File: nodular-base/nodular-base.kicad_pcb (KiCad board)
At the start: 2 copper layers, 83.1 x 92.5 mm, 18 parts, among them J1 Conn_02x10_Counter_Clockwise, J2 Conn_02x10_Counter_Clockwise, J3 Conn_02x10_Counter_Clockwise, J4 Conn_02x10_Counter_Clockwise, J5 Conn_02x10_Counter_Clockwise, J6 Conn_02x10_Counter_Clockwise

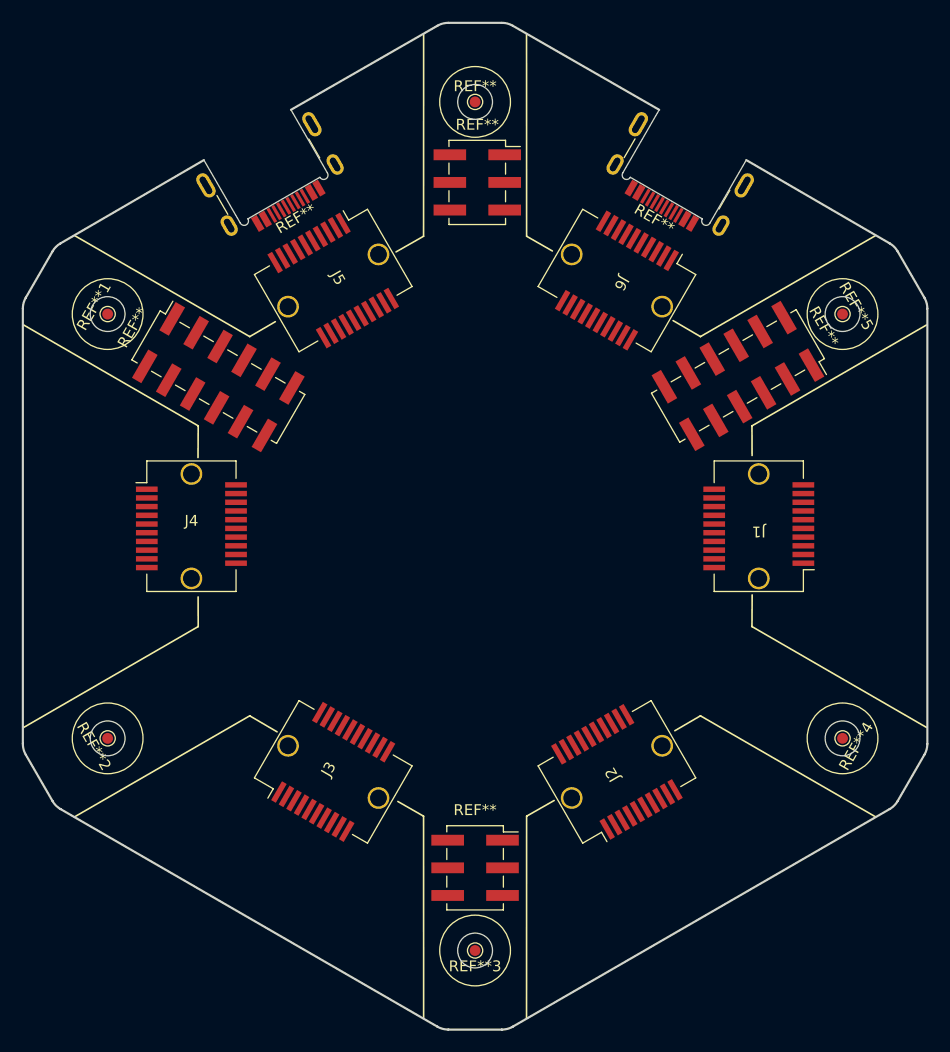
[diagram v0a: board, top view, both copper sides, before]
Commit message: more solderable standoffs, mid-mount USB
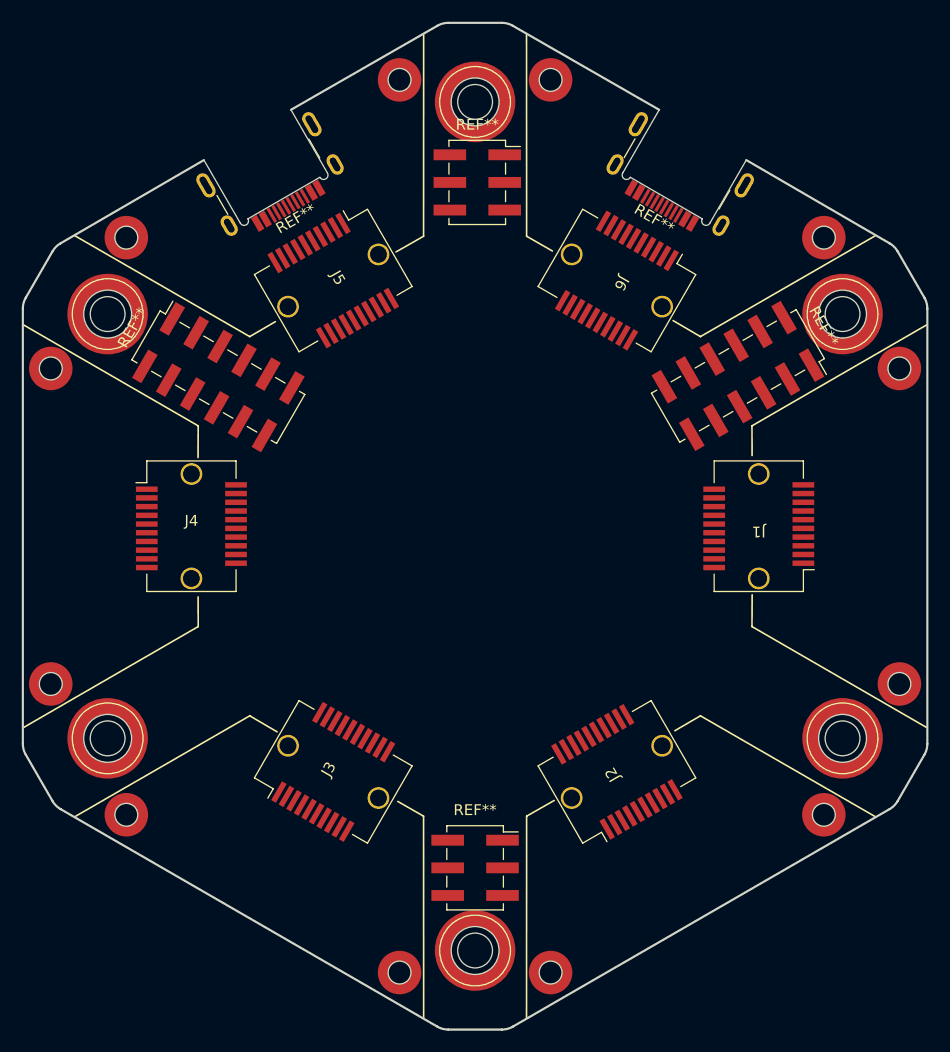
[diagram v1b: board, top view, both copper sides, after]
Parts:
- removed the REF** at (100.0, 61.0)
- added REF**: Mounting_Wuerth_WA-SMSI-M3_H12mm_9774120360, Mounting_Wuerth:Mounting_Wuerth_WA-SMSI-M3_H12mm_9774120360, F.Cu at (100.0, 61.0)
- added REF**: Mounting_Wuerth_WA-SMSI-M1.6_H2.5mm_9774025633, Mounting_Wuerth:Mounting_Wuerth_WA-SMSI-M1.6_H2.5mm_9774025633, F.Cu at (139.0, 114.5)
- added REF**: Mounting_Wuerth_WA-SMSI-M1.6_H2.5mm_9774025633, Mounting_Wuerth:Mounting_Wuerth_WA-SMSI-M1.6_H2.5mm_9774025633, F.Cu at (139.0, 85.5)
- added REF**10: Mounting_Wuerth_WA-SMSI-M1.6_H2.5mm_9774025633, Mounting_Wuerth:Mounting_Wuerth_WA-SMSI-M1.6_H2.5mm_9774025633, F.Cu at (61.0, 114.5)
- added REF**11: Mounting_Wuerth_WA-SMSI-M1.6_H2.5mm_9774025633, Mounting_Wuerth:Mounting_Wuerth_WA-SMSI-M1.6_H2.5mm_9774025633, F.Cu at (61.0, 85.5)
- added REF**12: Mounting_Wuerth_WA-SMSI-M1.6_H2.5mm_9774025633, Mounting_Wuerth:Mounting_Wuerth_WA-SMSI-M1.6_H2.5mm_9774025633, F.Cu at (93.1, 141.0)
- added REF**13: Mounting_Wuerth_WA-SMSI-M1.6_H2.5mm_9774025633, Mounting_Wuerth:Mounting_Wuerth_WA-SMSI-M1.6_H2.5mm_9774025633, F.Cu at (67.9, 126.5)
- added REF**14: Mounting_Wuerth_WA-SMSI-M1.6_H2.5mm_9774025633, Mounting_Wuerth:Mounting_Wuerth_WA-SMSI-M1.6_H2.5mm_9774025633, F.Cu at (106.9, 141.0)
- added REF**15: Mounting_Wuerth_WA-SMSI-M1.6_H2.5mm_9774025633, Mounting_Wuerth:Mounting_Wuerth_WA-SMSI-M1.6_H2.5mm_9774025633, F.Cu at (132.1, 126.5)
- added REF**6: Mounting_Wuerth_WA-SMSI-M1.6_H2.5mm_9774025633, Mounting_Wuerth:Mounting_Wuerth_WA-SMSI-M1.6_H2.5mm_9774025633, F.Cu at (132.1, 73.5)
- added REF**7: Mounting_Wuerth_WA-SMSI-M1.6_H2.5mm_9774025633, Mounting_Wuerth:Mounting_Wuerth_WA-SMSI-M1.6_H2.5mm_9774025633, F.Cu at (106.9, 59.0)
- added REF**8: Mounting_Wuerth_WA-SMSI-M1.6_H2.5mm_9774025633, Mounting_Wuerth:Mounting_Wuerth_WA-SMSI-M1.6_H2.5mm_9774025633, F.Cu at (67.9, 73.5)
- added REF**9: Mounting_Wuerth_WA-SMSI-M1.6_H2.5mm_9774025633, Mounting_Wuerth:Mounting_Wuerth_WA-SMSI-M1.6_H2.5mm_9774025633, F.Cu at (93.1, 59.0)
- REF**1, REF**2, REF**3, REF**4, REF**5: value TestPoint_Pad_D1.0mm -> Mounting_Wuerth_WA-SMSI-M3_H12mm_9774120360; footprint TestPoint:TestPoint_Pad_D1.0mm -> Mounting_Wuerth:Mounting_Wuerth_WA-SMSI-M3_H12mm_9774120360

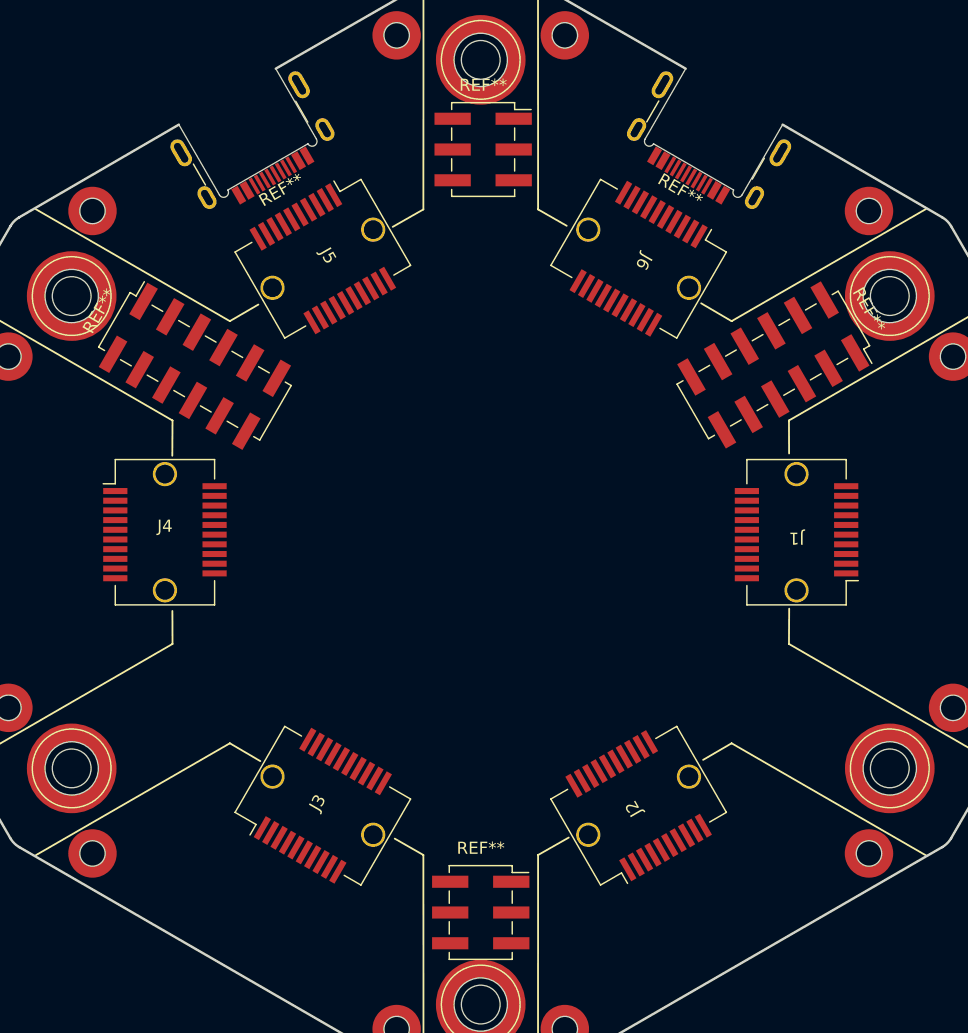
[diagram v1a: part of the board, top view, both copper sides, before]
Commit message: Update layout for top board, add library items
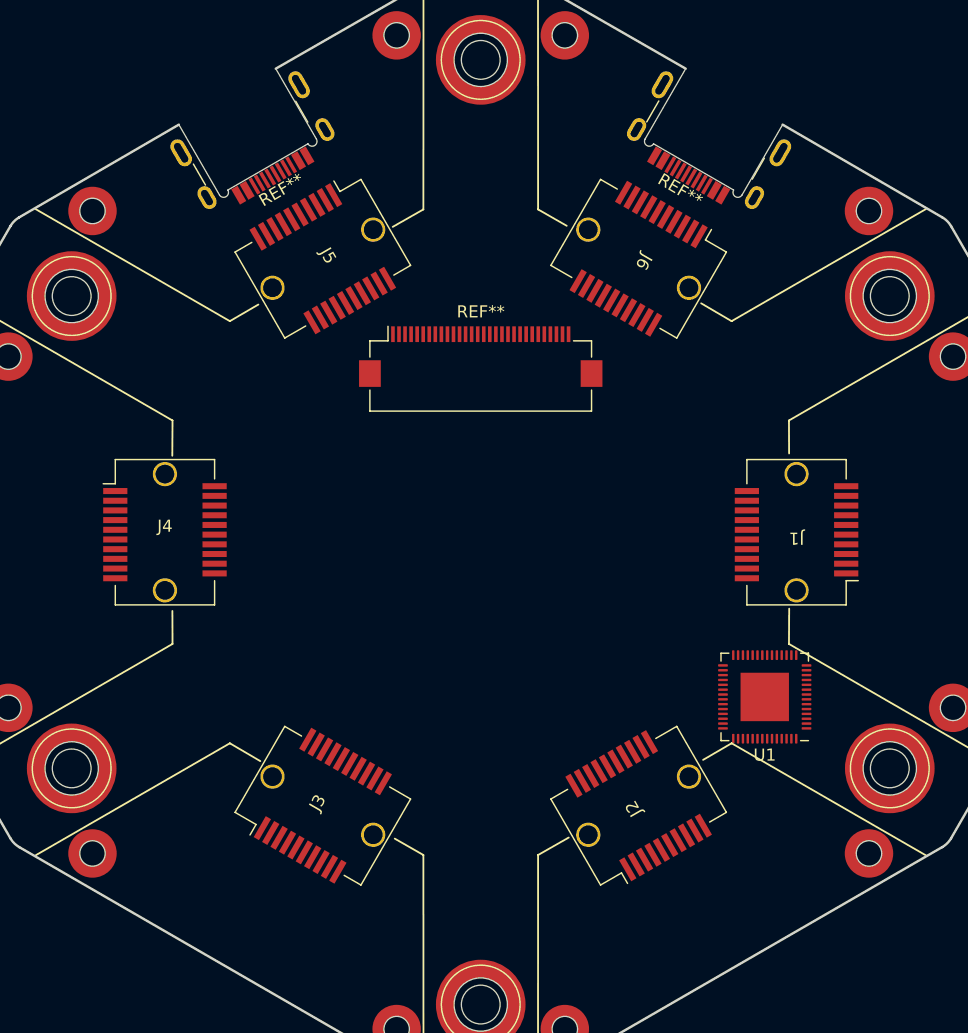
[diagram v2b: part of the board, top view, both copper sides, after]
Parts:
- removed the REF** at (124.2, 86.2)
- removed the REF** at (100.0, 131.4)
- removed the REF** at (100.2, 68.4)
- removed the REF** at (76.4, 86.3)
- added REF**: Hirose_FH12-30S-0.5SH_1x30-1MP_P0.50mm_Horizontal, Connector_FFC-FPC:Hirose_FH12-30S-0.5SH_1x30-1MP_P0.50mm_Horizontal, F.Cu at (100.0, 85.5)
- added U1: ESP32-S3-PICO-1-N8R2, Package_DFN_QFN:QFN-56-1EP_7x7mm_P0.4mm_EP4x4mm, F.Cu at (123.5, 113.6)
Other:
- board text added: "Display header top"

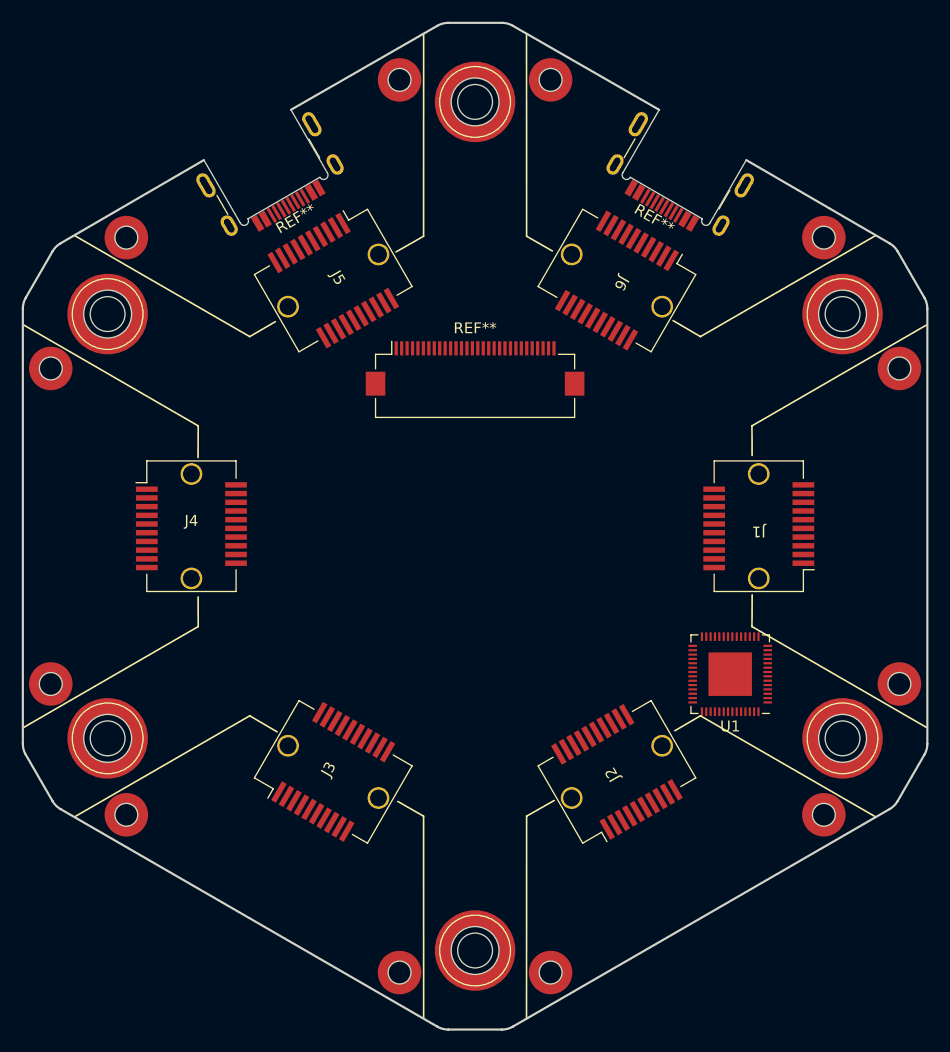
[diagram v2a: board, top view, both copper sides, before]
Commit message: Nodular-base: Add most components onto baseboard for a test fit. Nodular-base: Add fps and models for solderable standoffs, replace solderable standoffs and reposition them. Nodule template: Adjust nodule template hole position, export STEP of nodule. Nodular-base: Add many components to schematic, structure schematic hierarchy Nodular-base: Route USB, RF path, and MCU decoupling
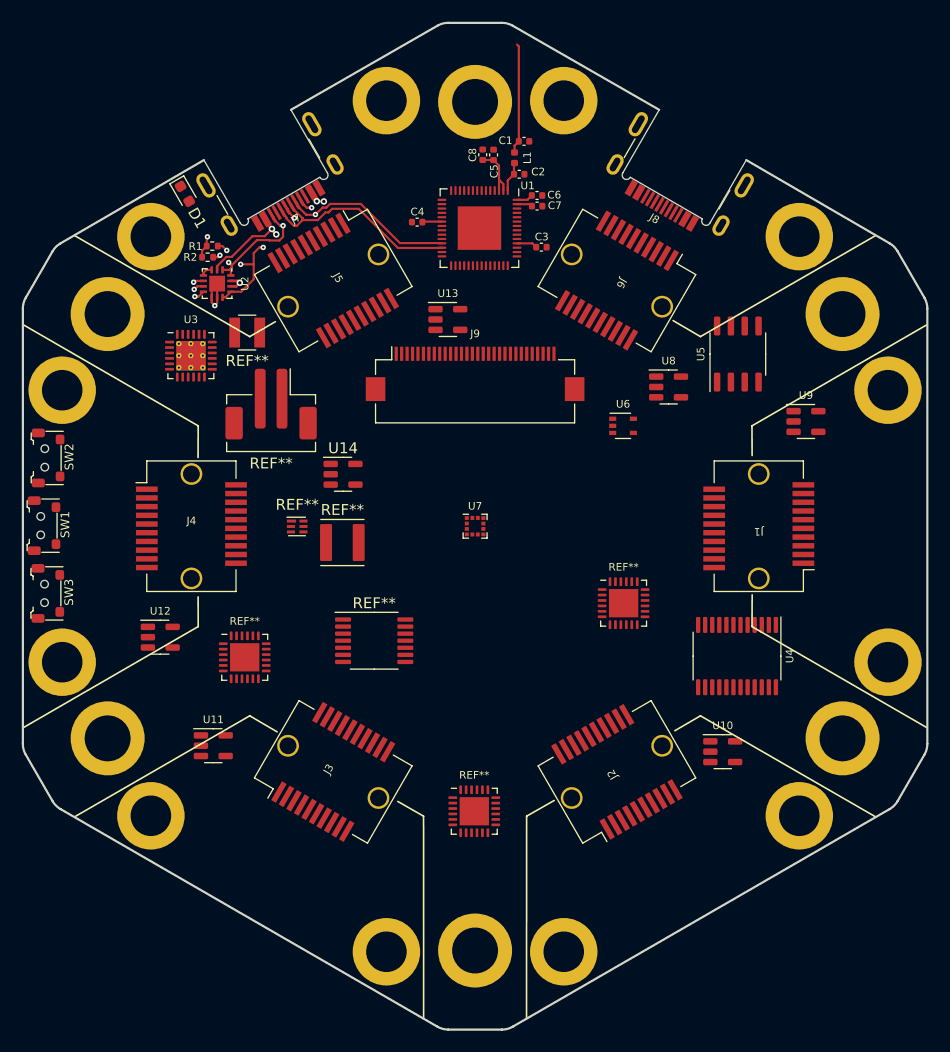
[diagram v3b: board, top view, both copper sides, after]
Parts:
- removed the REF** at (100.0, 85.5)
- removed the REF** at (100.0, 61.0)
- removed the REF** at (139.0, 114.5)
- removed the REF** at (139.0, 85.5)
- removed REF**1, REF**2, REF**3, REF**4, REF**5: Mounting_Wuerth_WA-SMSI-M3_H12mm_9774120360, Mounting_Wuerth:Mounting_Wuerth_WA-SMSI-M3_H12mm_9774120360
- removed REF**10, REF**11, REF**12, REF**13, REF**14, REF**15, REF**6, REF**7, REF**8, REF**9: Mounting_Wuerth_WA-SMSI-M1.6_H2.5mm_9774025633, Mounting_Wuerth:Mounting_Wuerth_WA-SMSI-M1.6_H2.5mm_9774025633
- added C1: C, Capacitor_SMD:C_0402_1005Metric, F.Cu at (104.5, 64.6)
- added C2: C, Capacitor_SMD:C_0402_1005Metric, F.Cu at (104.1, 67.7)
- added C3: 100nF, Capacitor_SMD:C_0402_1005Metric, F.Cu at (106.1, 74.3)
- added C4: 100nF, Capacitor_SMD:C_0402_1005Metric, F.Cu at (94.7, 72.0)
- added C5: 100nF, Capacitor_SMD:C_0402_1005Metric, F.Cu at (101.7, 65.9)
- added C6: 100nF, Capacitor_SMD:C_0402_1005Metric, F.Cu at (105.7, 69.6)
- added C7: 100nF, Capacitor_SMD:C_0402_1005Metric, F.Cu at (105.7, 70.6)
- added C8: 100nF, Capacitor_SMD:C_0402_1005Metric, F.Cu at (100.7, 65.9)
- added D1: LED, LED_SMD:LED_0603_1608Metric, F.Cu at (73.3, 69.5)
- added H1: MountingHole_Pad, nodular:SMTSO2030CTJ, F.Cu at (137.9, 87.5)
- added H10: MountingHole_Pad, nodular:SMTSO2030CTJ, F.Cu at (91.9, 60.9)
- added H11: MountingHole_Pad, nodular:SMTSO2030CTJ, F.Cu at (108.1, 60.9)
- added H12: MountingHole_Pad, nodular:SMTSO2030CTJ, F.Cu at (129.8, 73.4)
- added H13: MountingHole_Pad, nodular:SMTSO3030CTJ, F.Cu at (100.0, 61.0)
- added H14: MountingHole_Pad, nodular:SMTSO3030CTJ, F.Cu at (66.2, 80.5)
- added H15: MountingHole_Pad, nodular:SMTSO3030CTJ, F.Cu at (66.2, 119.5)
- added H16: MountingHole_Pad, nodular:SMTSO3030CTJ, F.Cu at (100.0, 139.0)
- added H17: MountingHole_Pad, nodular:SMTSO3030CTJ, F.Cu at (133.8, 119.5)
- added H18: MountingHole_Pad, nodular:SMTSO3030CTJ, F.Cu at (133.8, 80.5)
- added H2: MountingHole_Pad, nodular:SMTSO2030CTJ, F.Cu at (137.9, 112.5)
- added H3: MountingHole_Pad, nodular:SMTSO2030CTJ, F.Cu at (129.8, 126.6)
- added H4: MountingHole_Pad, nodular:SMTSO2030CTJ, F.Cu at (108.1, 139.1)
- added H5: MountingHole_Pad, nodular:SMTSO2030CTJ, F.Cu at (91.9, 139.1)
- added H6: MountingHole_Pad, nodular:SMTSO2030CTJ, F.Cu at (70.2, 126.6)
- added H7: MountingHole_Pad, nodular:SMTSO2030CTJ, F.Cu at (62.0, 112.5)
- added H8: MountingHole_Pad, nodular:SMTSO2030CTJ, F.Cu at (62.0, 87.5)
- added H9: MountingHole_Pad, nodular:SMTSO2030CTJ, F.Cu at (70.2, 73.4)
- added J9: Conn_01x30_MountingPin, Connector_FFC-FPC:Hirose_FH12-30S-0.5SH_1x30-1MP_P0.50mm_Horizontal, F.Cu at (100.0, 86.0)
- added L1: L, Inductor_SMD:L_0402_1005Metric, F.Cu at (103.6, 66.1)
- added R1: 5k1, Resistor_SMD:R_0402_1005Metric, F.Cu at (75.8, 74.2)
- added R2: 5k1, Resistor_SMD:R_0402_1005Metric, F.Cu at (75.4, 75.3)
- added REF**: QFN-24-1EP_4x4mm_P0.5mm_EP2.7x2.6mm, Package_DFN_QFN:QFN-24-1EP_4x4mm_P0.5mm_EP2.7x2.6mm, F.Cu at (99.9, 126.2)
- added REF**: WSON6_1.5x1.5mm_P0.5mm, Package_SON:WSON-6_1.5x1.5mm_P0.5mm, F.Cu at (83.7, 100.0)
- added REF**: TSSOP-14_4.4x5mm_P0.65mm, Package_SO:TSSOP-14_4.4x5mm_P0.65mm, F.Cu at (90.7, 110.5)
- added REF**: QFN-24-1EP_4x4mm_P0.5mm_EP2.7x2.6mm, Package_DFN_QFN:QFN-24-1EP_4x4mm_P0.5mm_EP2.7x2.6mm, F.Cu at (113.7, 107.1)
- added REF**: QFN-24-1EP_4x4mm_P0.5mm_EP2.7x2.6mm, Package_DFN_QFN:QFN-24-1EP_4x4mm_P0.5mm_EP2.7x2.6mm, F.Cu at (78.8, 112.0)
- added REF**: JST_PH_B2B-PH-SM4-TB_1x02-1MP_P2.00mm_Vertical, Connector_JST:JST_PH_B2B-PH-SM4-TB_1x02-1MP_P2.00mm_Vertical, F.Cu at (81.2, 88.8)
- added REF**: L_Abracon_ASPI-4030S, Inductor_SMD:L_Abracon_ASPI-4030S, F.Cu at (87.8, 101.5)
- added REF**: L_Abracon_ASPI-3012S, Inductor_SMD:L_Abracon_ASPI-3012S, F.Cu at (79.0, 82.2)
- added SW1: SW_Push, nodular:sidebutton-1TS003B-1400-3500A-CT, F.Cu at (60.1, 100.0)
- added SW2: SW_Push, nodular:sidebutton-1TS003B-1400-3500A-CT, F.Cu at (60.5, 93.7)
- added SW3: SW_Push, nodular:sidebutton-1TS003B-1400-3500A-CT, F.Cu at (60.4, 106.2)
- added U10: MT9700, Package_TO_SOT_SMD:SOT-23-5, F.Cu at (122.8, 120.7)
- added U11: MT9700, Package_TO_SOT_SMD:SOT-23-5, F.Cu at (75.9, 120.2)
- added U12: MT9700, Package_TO_SOT_SMD:SOT-23-5, F.Cu at (71.1, 110.2)
- added U13: MT9700, Package_TO_SOT_SMD:SOT-23-5, F.Cu at (97.5, 81.0)
- added U14: MT9700, Package_TO_SOT_SMD:SOT-23-5, F.Cu at (87.9, 95.2)
- added U2: FUSB302BMPX, Package_DFN_QFN:WQFN-14-1EP_2.5x2.5mm_P0.5mm_EP1.45x1.45mm, F.Cu at (76.3, 77.7)
- added U3: BQ25895RTW, Package_DFN_QFN:Texas_S-PWQFN-N24_EP2.7x2.7mm_ThermalVias, F.Cu at (73.9, 84.3)
- added U4: TCA9548APWR, Package_SO:TSSOP-24_4.4x7.8mm_P0.65mm, F.Cu at (124.1, 111.9)
- added U5: MAX3051, Package_SO:SO-8_3.9x4.9mm_P1.27mm, F.Cu at (124.2, 84.2)
- added U6: 74LVC1G17, Package_TO_SOT_SMD:SOT-353_SC-70-5, F.Cu at (113.6, 90.8)
- added U7: SC7A20, Package_LGA:LGA-12_2x2mm_P0.5mm, F.Cu at (100.0, 100.0)
- added U8: MT9700, Package_TO_SOT_SMD:SOT-23-5, F.Cu at (117.8, 87.2)
- added U9: MT9700, Package_TO_SOT_SMD:SOT-23-5, F.Cu at (130.4, 90.4)
- J7, J8: renamed from REF**; value USB_C_Receptacle_SHOUHAN_TYPE-C_16P_CB1.6_073 -> USB_C_Receptacle_USB2.0
- moved U1 47.0 mm to (100.4, 72.6), turned to -90 degrees
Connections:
- J1 pad 1: unconnected-(J1-Pin_1-Pad1) -> GND
- J1 pad 10: unconnected-(J1-Pin_10-Pad10) -> GND
- J1 pad 11: unconnected-(J1-Pin_11-Pad11) -> GND
- J1 pad 14: unconnected-(J1-Pin_14-Pad14) -> GND
- J1 pad 17: unconnected-(J1-Pin_17-Pad17) -> GND
- J1 pad 20: unconnected-(J1-Pin_20-Pad20) -> GND
- J2 pad 1: unconnected-(J2-Pin_1-Pad1) -> GND
- J2 pad 10: unconnected-(J2-Pin_10-Pad10) -> GND
- J2 pad 11: unconnected-(J2-Pin_11-Pad11) -> GND
- J2 pad 14: unconnected-(J2-Pin_14-Pad14) -> GND
- J2 pad 17: unconnected-(J2-Pin_17-Pad17) -> GND
- J2 pad 20: unconnected-(J2-Pin_20-Pad20) -> GND
- J3 pad 1: unconnected-(J3-Pin_1-Pad1) -> GND
- J3 pad 10: unconnected-(J3-Pin_10-Pad10) -> GND
- J3 pad 11: unconnected-(J3-Pin_11-Pad11) -> GND
- J3 pad 14: unconnected-(J3-Pin_14-Pad14) -> GND
- J3 pad 17: unconnected-(J3-Pin_17-Pad17) -> GND
- J3 pad 20: unconnected-(J3-Pin_20-Pad20) -> GND
- J4 pad 1: unconnected-(J4-Pin_1-Pad1) -> GND
- J4 pad 10: unconnected-(J4-Pin_10-Pad10) -> GND
- J4 pad 11: unconnected-(J4-Pin_11-Pad11) -> GND
- J4 pad 14: unconnected-(J4-Pin_14-Pad14) -> GND
- J4 pad 17: unconnected-(J4-Pin_17-Pad17) -> GND
- J4 pad 20: unconnected-(J4-Pin_20-Pad20) -> GND
- J5 pad 1: unconnected-(J5-Pin_1-Pad1) -> GND
- J5 pad 10: unconnected-(J5-Pin_10-Pad10) -> GND
- J5 pad 11: unconnected-(J5-Pin_11-Pad11) -> GND
- J5 pad 14: unconnected-(J5-Pin_14-Pad14) -> GND
- J5 pad 17: unconnected-(J5-Pin_17-Pad17) -> GND
- J5 pad 20: unconnected-(J5-Pin_20-Pad20) -> GND
- J6 pad 1: unconnected-(J6-Pin_1-Pad1) -> GND
- J6 pad 10: unconnected-(J6-Pin_10-Pad10) -> GND
- J6 pad 11: unconnected-(J6-Pin_11-Pad11) -> GND
- J6 pad 14: unconnected-(J6-Pin_14-Pad14) -> GND
- J6 pad 17: unconnected-(J6-Pin_17-Pad17) -> GND
- J6 pad 20: unconnected-(J6-Pin_20-Pad20) -> GND
- J7 pad A1: (no net) -> GND
- J7 pad A12: (no net) -> GND
- J7 pad A4: (no net) -> Net-(U2-VBUS)
- J7 pad A5: (no net) -> Net-(J7-CC1)
- J7 pad A6: (no net) -> /USB+
- J7 pad A7: (no net) -> /USB-
- J7 pad A8: (no net) -> unconnected-(J7-SBU1-PadA8)
- J7 pad A9: (no net) -> Net-(U2-VBUS)
- J7 pad B1: (no net) -> GND
- J7 pad B12: (no net) -> GND
- J7 pad B4: (no net) -> Net-(U2-VBUS)
- J7 pad B5: (no net) -> Net-(J7-CC2)
- J7 pad B6: (no net) -> /USB+
- J7 pad B7: (no net) -> /USB-
- J7 pad B8: (no net) -> unconnected-(J7-SBU2-PadB8)
- J7 pad B9: (no net) -> Net-(U2-VBUS)
- J7 pad S1: (no net) -> GND
- J8 pad A1: (no net) -> Net-(J8-GND-PadA1)
- J8 pad A12: (no net) -> Net-(J8-GND-PadA1)
- J8 pad A4: (no net) -> Net-(J8-VBUS-PadA4)
- J8 pad A5: (no net) -> unconnected-(J8-CC1-PadA5)
- J8 pad A6: (no net) -> unconnected-(J8-D+-PadA6)
- J8 pad A7: (no net) -> unconnected-(J8-D--PadA7)
- J8 pad A8: (no net) -> unconnected-(J8-SBU1-PadA8)
- J8 pad A9: (no net) -> Net-(J8-VBUS-PadA4)
- J8 pad B1: (no net) -> Net-(J8-GND-PadA1)
- J8 pad B12: (no net) -> Net-(J8-GND-PadA1)
- J8 pad B4: (no net) -> Net-(J8-VBUS-PadA4)
- J8 pad B5: (no net) -> unconnected-(J8-CC2-PadB5)
- J8 pad B6: (no net) -> unconnected-(J8-D+-PadB6)
- J8 pad B7: (no net) -> unconnected-(J8-D--PadB7)
- J8 pad B8: (no net) -> unconnected-(J8-SBU2-PadB8)
- J8 pad B9: (no net) -> Net-(J8-VBUS-PadA4)
- J8 pad S1: (no net) -> unconnected-(J8-SHIELD-PadS1)
- U1 pad 1: unconnected-(U1-LNA_IN-Pad1) -> Net-(U1-LNA_IN)
- U1 pad 2: Net-(U1-VDD3P3-Pad2) -> Net-(U1-VDD3P3_CPU)
- U1 pad 20: unconnected-(U1-VDD3P3_RTC-Pad20) -> Net-(U1-VDD3P3_CPU)
- U1 pad 25: unconnected-(U1-GPIO19/USBDM-Pad25) -> /USB-
- U1 pad 26: unconnected-(U1-GPIO20/USBDP-Pad26) -> /USB+
- U1 pad 3: Net-(U1-VDD3P3-Pad2) -> Net-(U1-VDD3P3_CPU)
- U1 pad 46: unconnected-(U1-VDD3P3_CPU-Pad46) -> Net-(U1-VDD3P3_CPU)
- U1 pad 55: Net-(U1-VDDA-Pad55) -> Net-(U1-VDD3P3_CPU)
- U1 pad 56: Net-(U1-VDDA-Pad55) -> Net-(U1-VDD3P3_CPU)
- U1 pad 57: (no net) -> GND
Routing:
- net Net-(J7-CC1): track 0.00 -> 20.5 mm, vias 0 -> 4
- net /USB-: track 0.00 -> 19.4 mm, vias 0 -> 2
- net /USB+: track 0.00 -> 19.4 mm
- net Net-(U2-VBUS): track 0.00 -> 17.5 mm, vias 0 -> 4
- net Net-(J7-CC2): track 0.00 -> 12.3 mm, vias 0 -> 3
- net Net-(U1-VDD3P3_CPU): track 0.00 -> 11.9 mm
- net Net-(C1-Pad1): track 0.00 -> 10.2 mm
- net Net-(U2-GND-Pad15): track 0.00 -> 4.46 mm, vias 0 -> 1
- net Net-(U1-LNA_IN): track 0.00 -> 2.79 mm
- net GND: track 0.00 -> 2.08 mm, vias 0 -> 1
- net Net-(U2-VCONN-Pad12): track 0.00 -> 1.86 mm, vias 0 -> 1
- net Net-(U2-VDD-Pad3): track 0.00 -> 1.11 mm
- net unconnected-(U2-SDA-Pad7): track 0.00 -> 0.97 mm, vias 0 -> 1
- net unconnected-(U2-SCL-Pad6): track 0.00 -> 0.96 mm, vias 0 -> 1
- net unconnected-(U2-INT_N-Pad5): track 0.00 -> 0.95 mm, vias 0 -> 1
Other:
- outline, holes or cut-outs redrawn
- copper layers 2 -> 4
